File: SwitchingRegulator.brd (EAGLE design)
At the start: 119.4 x 100 mm, 30 parts, among them J1 APP_2POS_CONFIG5V_HORIZ, J2 APP_2POS_CONFIG5V_HORIZ, J3 APP_2POS_CONFIG5V_HORIZ, Q2 Q_CSD18532KCSPCB, Q3 Q_CSD18532KCSPCB, U1 OKI-78SR-5/1.5-W36HC

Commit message: Board design initiated
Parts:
- CDRVCC: device SparkFun-Passives:EIA3216 -> SparkFun-Passives:0603-CAP
- moved Q3 228.7 mm to (111.8, 64.8)
- moved Q2 183.0 mm to (85.1, 64.8)
- moved U$1 153.7 mm to (62.2, 50.8), turned to 270 degrees
- moved CIN2 149.7 mm to (108.2, 83.1)
- moved RF 146.0 mm to (70.6, 51.1), turned to 180 degrees
- moved C1 142.2 mm to (62.2, 62.5)
- moved CIN1 139.5 mm to (98.6, 56.4), turned to 90 degrees
- moved RSET 138.0 mm to (55.4, 53.6)
- moved RMAX 135.5 mm to (55.4, 50.5)
- moved CVCC 134.0 mm to (73.9, 43.9), turned to 270 degrees
- moved C3 129.9 mm to (107.7, 86.6)
- moved RC2 119.3 mm to (43.9, 47.2), turned to 180 degrees
- moved RC1 118.3 mm to (47.8, 49.5)
- moved R2 115.9 mm to (47.8, 47.2)
- moved CSS 112.1 mm to (55.4, 48.0), turned to 180 degrees
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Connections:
- net GND: now also CDRVCC.2; no longer CDRVCC.C
- net N$15: now also CDRVCC.1; no longer CDRVCC.A

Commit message: Revision 1 routing complete
LTC3703-5 datasheet provided a list of constraints that had to be worked around.  Ground plane separated into a signal ground and a power ground.  Some components needed to be placed close to the IC as well causing some suboptimal routes.
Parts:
- moved D1 208.0 mm to (81.3, 34.3), turned to 90 degrees
- moved U1 188.0 mm to (35.8, 60.2), turned to 180 degrees
- moved DB 169.8 mm to (32.5, 38.9), turned to 90 degrees
- moved L1 158.9 mm to (48.8, 35.8), turned to 270 degrees
- moved COUT2 119.7 mm to (24.9, 10.9), turned to 270 degrees
- moved C3 117.8 mm to (25.7, 2.03), turned to 180 degrees
- moved J2 109.9 mm to (8.38, -9.91), turned to 90 degrees
- moved COUT1 100.5 mm to (24.9, 24.1), turned to 270 degrees
- moved J1 76.0 mm to (16.5, -9.91), turned to 90 degrees
- moved Q3 61.1 mm to (51.6, 54.4)
- moved J3 58.9 mm to (3.05, 84.3), turned to 270 degrees
- moved CIN2 51.7 mm to (66.0, 53.1), turned to 180 degrees
- moved CVCC 47.3 mm to (27.7, 33.8)
- moved CC3 44.3 mm to (5.59, 31.5), turned to 0 degrees
- moved RMAX 42.8 mm to (16.0, 33.8)
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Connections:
- net GND: now also CIN1.GND, COUT1.GND, COUT2.GND; no longer CIN1.-, COUT1.-, COUT2.-
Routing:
- net N$2: track 0.00 -> 62.9 mm, vias 0 -> 4
- net GND: track 0.00 -> 53.4 mm, vias 0 -> 8
- net N$5: track 0.00 -> 51.4 mm, vias 0 -> 2
- net N$16: track 0.00 -> 34.7 mm, vias 0 -> 2
- net N$15: track 0.00 -> 29.7 mm
- net N$11: track 0.00 -> 19.5 mm
- net VBATT: track 0.00 -> 14.7 mm
- net N$17: track 0.00 -> 13.9 mm
- net N$7: track 0.00 -> 9.79 mm
- net N$13: track 0.00 -> 6.84 mm
- net N$12: track 0.00 -> 6.63 mm
- net N$1: track 0.00 -> 5.77 mm
- net N$6: track 0.00 -> 4.46 mm
- net N$10: track 0.00 -> 4.27 mm
- net N$4: track 0.00 -> 3.69 mm
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- added copper zone on layer 16, net GND
- added copper zone on layer 1, net N$17
- added copper zone on layer 1, net VBATT
- added copper zone on layer 1, net VOUT12+
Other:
- board size 119.4 x 100 mm -> 92.2 x 74.3 mm

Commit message: Major rearrangements
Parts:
- D1: value RB160MM-30TR -> RBR3MM30ATR
- moved Q2 50.7 mm to (31.5, 70.6)
- moved D1 46.6 mm to (38.9, 53.6), turned to 270 degrees
- moved CIN1 21.6 mm to (44.5, 45.2)
- moved CIN2 19.1 mm to (47.0, 53.1), turned to 90 degrees
- moved Q3 17.7 mm to (44.5, 70.6)
- moved U1 15.5 mm to (20.6, 62.7), turned to 0 degrees
- moved C1 10.8 mm to (23.1, 36.6)
- moved CDRVCC 10.7 mm to (30.1, 44.5)
- moved CVCC 10.7 mm to (27.7, 44.5)
- moved R2 10.7 mm to (10.9, 44.5)
- moved RC2 10.7 mm to (5.59, 44.5)
- moved RMAX 10.7 mm to (16.0, 44.5)
- moved CC3 10.7 mm to (5.59, 42.2)
- moved CSS 10.7 mm to (16.0, 42.2)
- moved R1 10.7 mm to (10.9, 42.2)
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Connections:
- removed net N$12: CC3.2, R1.1
- removed net N$5: C1.+, DB.P$2, U$1.1, U1.3
- net N$15: now also C1.+, DB.P$2, U$1.1, U1.3
- net VOUT12+: now also CC3.2, R1.1
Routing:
- net N$2: track 62.9 -> 0.00 mm, vias 4 -> 0
- net N$5: track 51.4 -> 0.00 mm, vias 2 -> 0
- net N$16: track 34.7 -> 0.00 mm, vias 2 -> 0
- net GND: track 53.4 -> 26.8 mm, vias 8 -> 5
- net VOUT12+: track 0.00 -> 26.2 mm
- net VBATT: track 14.7 -> 0.00 mm
- net N$17: track 13.9 -> 23.6 mm
- net N$12: track 6.63 -> 0.00 mm
- net N$15: track 29.7 -> 34.8 mm
- removed copper zone on layer 1, net VBATT
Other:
- board size 92.2 x 74.3 mm -> 102.6 x 78.7 mm

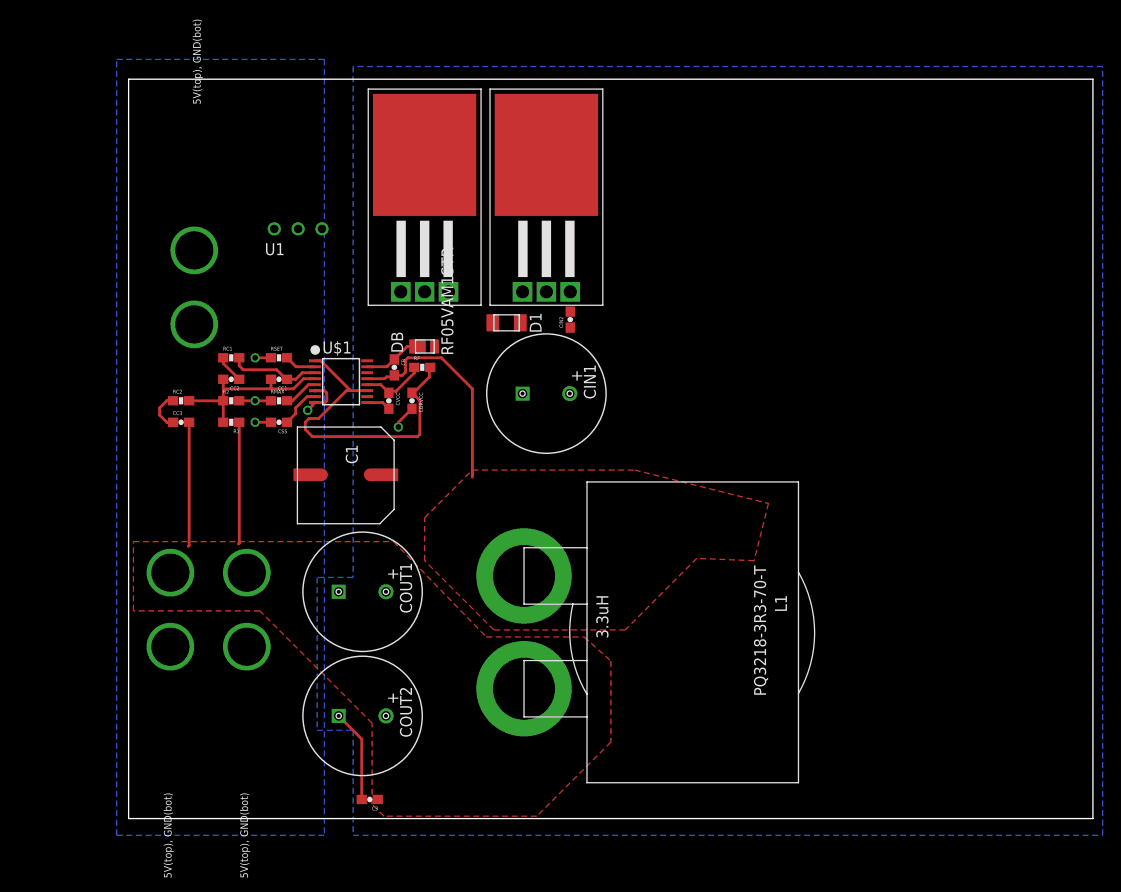
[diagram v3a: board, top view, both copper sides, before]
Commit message: Reconfigured board, still doesn't support 40A
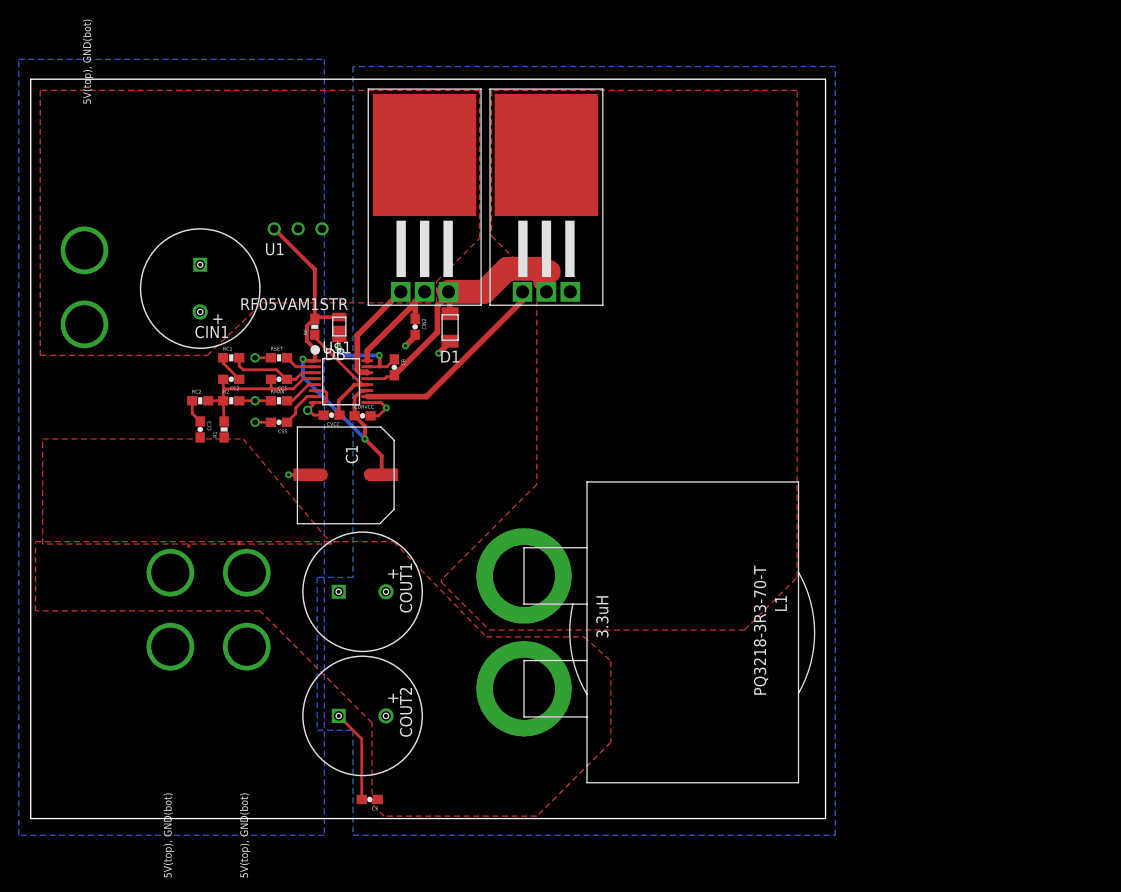
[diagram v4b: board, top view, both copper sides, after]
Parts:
- moved CIN1 38.5 mm to (7.62, 56.4), turned to 180 degrees
- moved CIN2 16.5 mm to (30.5, 52.3), turned to 270 degrees
- moved RF 12.2 mm to (19.8, 52.3), turned to 90 degrees
- moved J3 11.7 mm to (-8.64, 88.6)
- moved DB 10.1 mm to (23.1, 53.3), turned to 180 degrees
- moved CVCC 6.28 mm to (21.6, 42.9), turned to 180 degrees
- moved CDRVCC 5.50 mm to (24.9, 42.8), turned to 0 degrees
- moved D1 3.81 mm to (35.1, 53.6), turned to 180 degrees
- moved CC3 2.17 mm to (7.62, 41.4), turned to 270 degrees
- moved RC2 2.03 mm to (7.62, 44.5)
- moved R1 1.08 mm to (10.2, 41.4), turned to 90 degrees
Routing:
- net VOUT12+: track 26.2 -> 0.25 mm
- net N$16: track 0.00 -> 21.7 mm
- net VBATT: track 0.00 -> 11.7 mm
- net N$2: track 0.00 -> 11.4 mm
- net N$15: track 34.8 -> 43.6 mm, vias 0 -> 2
- net N$17: track 23.6 -> 30.4 mm
- net GND: track 26.8 -> 33.1 mm, vias 5 -> 8
- net N$13: track 6.84 -> 12.8 mm
- net N$1: track 5.77 -> 10.1 mm, vias 0 -> 2
- net N$11: track 19.5 -> 17.3 mm
- net N$10: track 4.27 -> 2.55 mm
- added copper zone on layer 1, net VBATT
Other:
- board size 102.6 x 78.7 mm -> 84.6 x 78.7 mm

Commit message: New layout, do power power path
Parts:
- removed J3: APP_2POS_CONFIG5V_HORIZ, MRDT-Connectors:APP45_5V_HORIZ_CONFIG
- added J4: APP_2POS_CONFIG12V_HORIZ, MRDT-Connectors:APP45_12V_HORIZ_CONFIG
- moved U1 59.8 mm to (78.2, 46.7)
- moved J1 49.2 mm to (-10.9, 31.0), turned to 0 degrees
- moved C3 39.3 mm to (31.5, 40.9)
- moved J2 38.2 mm to (-10.9, 23.1), turned to 0 degrees
- moved C1 35.9 mm to (33.0, 71.1)
- moved Q2 34.6 mm to (60.2, 51.3), flipped to the bottom
- moved U$1 30.0 mm to (52.6, 45.7), turned to 180 degrees
- moved COUT1 22.1 mm to (11.2, 6.86)
- moved Q3 19.3 mm to (44.2, 51.3), flipped to the bottom
- moved L1 18.7 mm to (62.0, 22.6), turned to 180 degrees
- moved COUT2 7.58 mm to (17.5, 12.7)
- moved CC1 0.72 mm to (16.5, 47.2)
- moved RSET 0.72 mm to (16.5, 49.5)
- moved CIN1 0.72 mm to (8.13, 56.9)
- moved CB 0.72 mm to (28.8, 48.5)
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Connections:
- net GND: now also J4.GND; no longer J3.GND
- net VBATT: now also J4.12V; no longer J3.5V
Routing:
- net N$15: track 43.6 -> 0.00 mm, vias 2 -> 0
- net GND: track 33.1 -> 0.00 mm, vias 8 -> 0
- net N$17: track 30.4 -> 0.00 mm
- net N$16: track 21.7 -> 0.00 mm
- net N$11: track 17.3 -> 0.00 mm
- net N$13: track 12.8 -> 0.00 mm
- net VBATT: track 11.7 -> 0.00 mm
- net N$2: track 11.4 -> 0.00 mm
- net N$1: track 10.1 -> 0.00 mm, vias 2 -> 0
- net N$7: track 9.79 -> 0.00 mm
- net N$6: track 4.46 -> 0.00 mm
- net N$4: track 3.69 -> 0.00 mm
- net N$3: track 3.64 -> 0.00 mm
- net N$9: track 2.99 -> 0.00 mm
- net N$10: track 2.55 -> 0.00 mm
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- added copper zone on layer 1, net GND
- added copper zone on layer 16, net N$17
- added copper zone on layer 16, net VBATT1
- added copper zone on layer 16, net VOUT12+

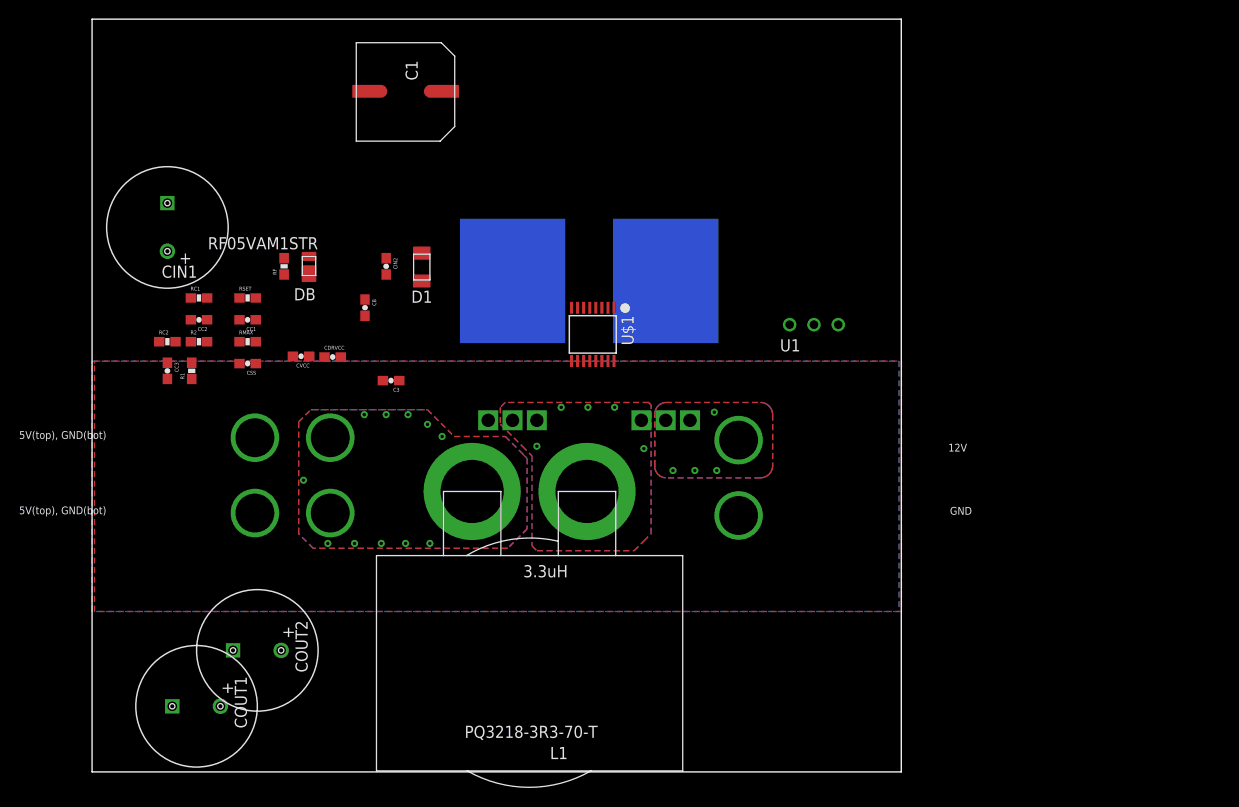
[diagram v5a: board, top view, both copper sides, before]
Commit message: Routing completed, needs to be approved
Added complete via stitching around all power traces.  Signal ground in lower right joined to power ground close to negative output terminal.  Sloppy routing under LTC chip, could be cleaner probably
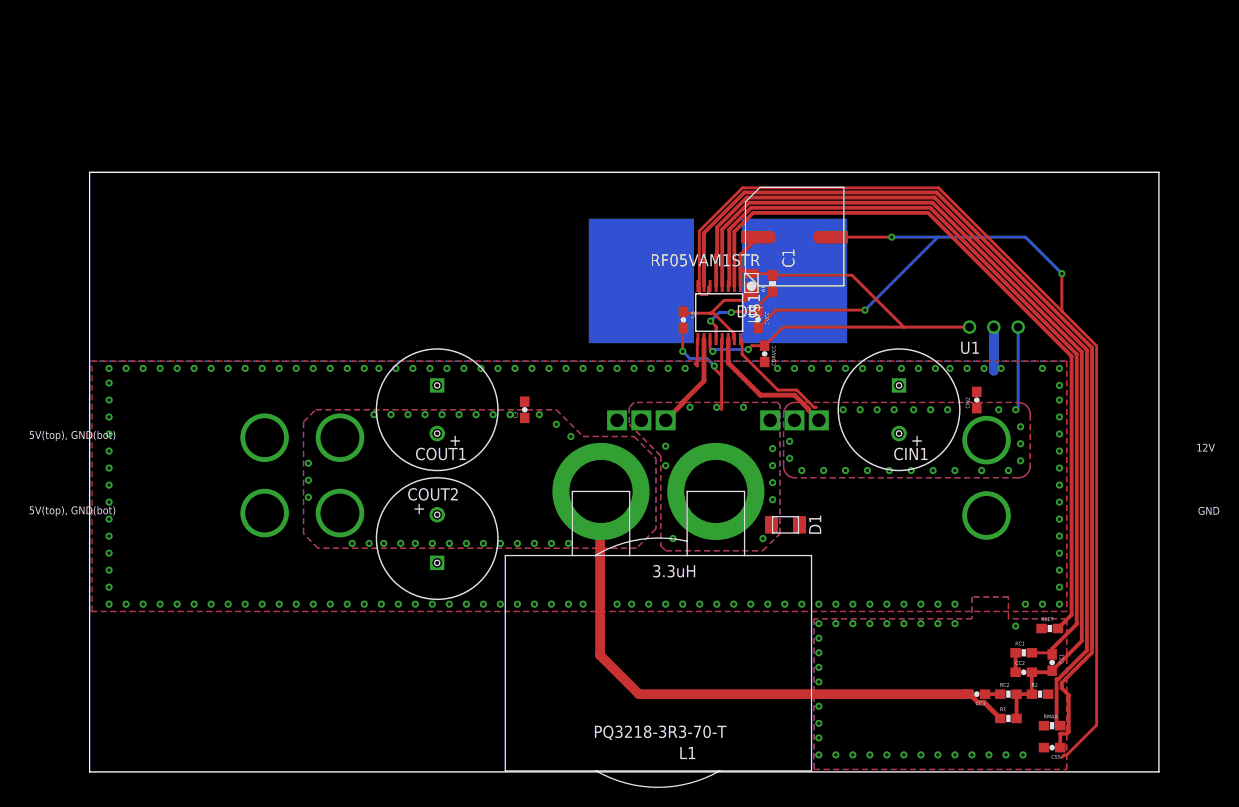
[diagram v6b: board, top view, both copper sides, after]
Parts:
- moved RC2 95.3 mm to (96.0, 8.13)
- moved R2 95.3 mm to (99.3, 8.13)
- moved RC1 93.8 mm to (97.6, 12.4)
- moved CC2 93.7 mm to (97.6, 10.4), turned to 0 degrees
- moved CSS 93.2 mm to (100.6, 2.54)
- moved RMAX 93.2 mm to (100.6, 4.83)
- moved R1 92.8 mm to (96.0, 5.59), turned to 0 degrees
- moved CC1 91.4 mm to (100.6, 11.4), turned to 270 degrees
- moved CC3 91.1 mm to (92.7, 8.13), turned to 180 degrees
- moved RSET 90.7 mm to (100.3, 15.0)
- moved CIN1 78.8 mm to (84.6, 37.8)
- moved CIN2 63.3 mm to (92.7, 38.9), turned to 90 degrees
- moved RF 51.1 mm to (71.4, 51.1)
- moved CVCC 47.9 mm to (69.8, 47.2), turned to 270 degrees
- moved DB 46.3 mm to (69.8, 52.1)
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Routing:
- net GND: track 0.00 -> 163.7 mm, vias 0 -> 163
- net N$6: track 0.00 -> 98.7 mm
- net N$11: track 0.00 -> 94.3 mm
- net N$4: track 0.00 -> 93.5 mm
- net N$7: track 0.00 -> 84.1 mm
- net N$3: track 0.00 -> 77.0 mm
- net VOUT12+: track 0.00 -> 61.7 mm, vias 2 -> 29
- net N$15: track 0.00 -> 55.4 mm, vias 0 -> 2
- net VBATT: track 0.00 -> 20.3 mm, vias 0 -> 24
- net N$17: track 0.00 -> 15.2 mm, vias 0 -> 13
- net N$2: track 0.00 -> 14.5 mm
- net N$1: track 0.00 -> 12.0 mm
- net N$13: track 0.00 -> 10.3 mm, vias 0 -> 2
- net N$16: track 0.00 -> 10.1 mm
- net N$9: track 0.00 -> 2.03 mm
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- added copper zone on layer 16, net VBATT
- removed copper zone on layer 16, net VBATT1
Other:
- board size 84.6 x 78.7 mm -> 111.7 x 62.7 mm
